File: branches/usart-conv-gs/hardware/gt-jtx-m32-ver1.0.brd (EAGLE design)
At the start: 59.4 x 64.8 mm, 29 parts, among them IC1 MEGA32-P

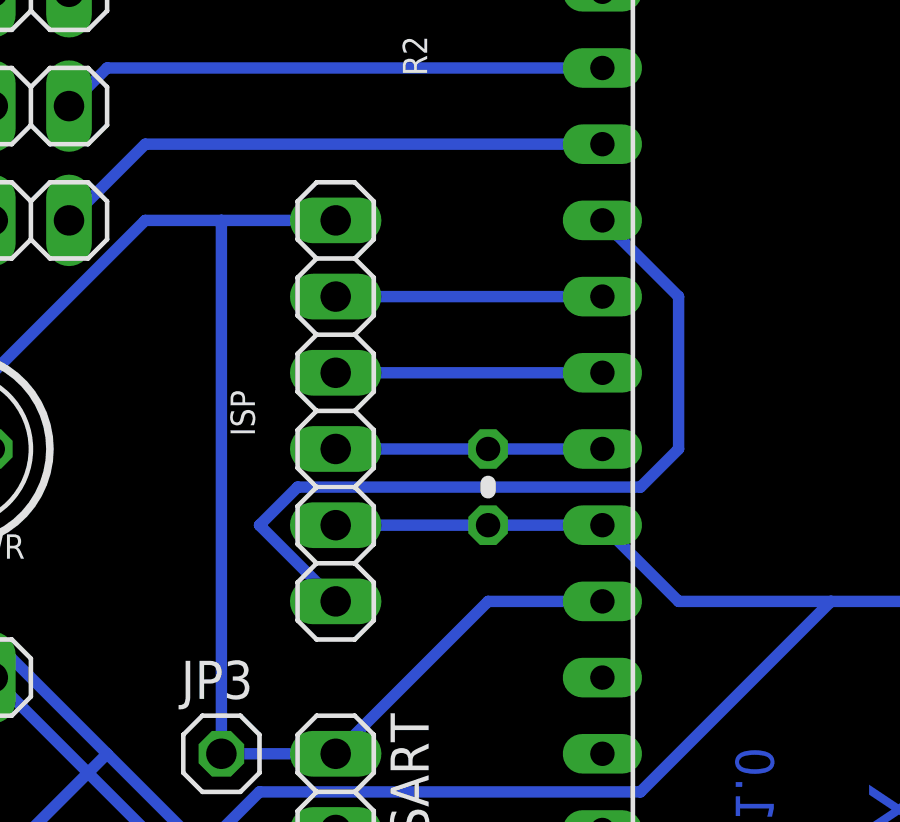
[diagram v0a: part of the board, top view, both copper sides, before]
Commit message: changed pin header to 3x2 instead of 1x6 for accomodating a 6 pin isp. correctec pin configurations
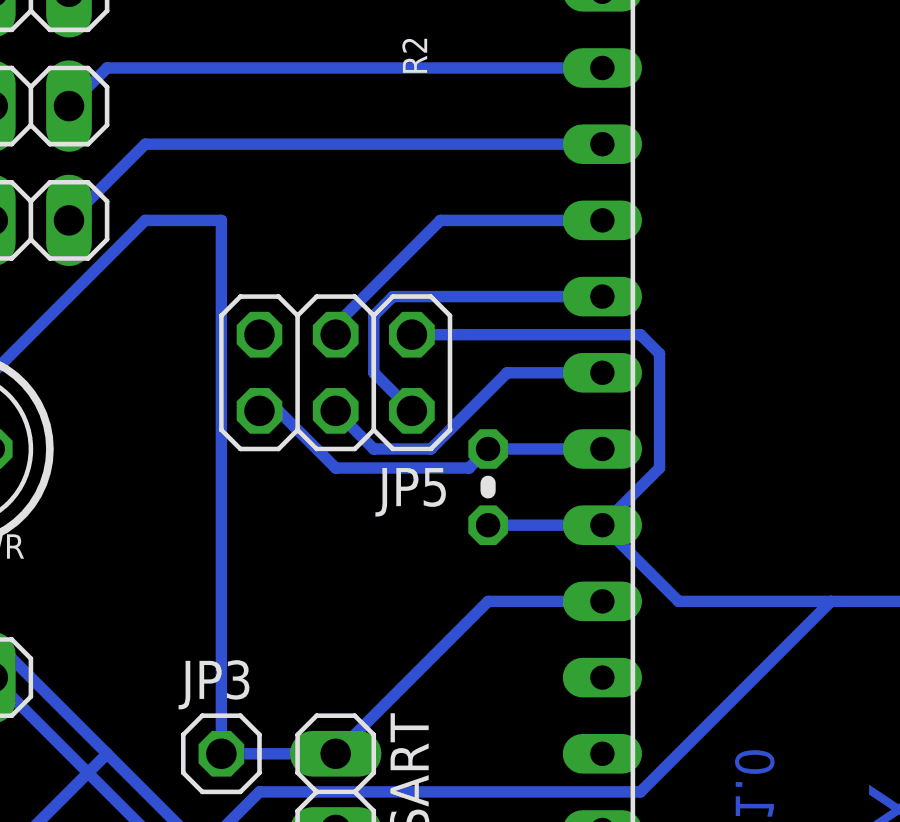
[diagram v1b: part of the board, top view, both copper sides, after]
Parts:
- removed ISP: (no value), pinhead:1X06
- added JP5: (no value), pinhead:2X03
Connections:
- net +5V: now also JP5.1; no longer ISP.2
- net GND: now also JP5.5; no longer ISP.6
- net N$12: now also JP5.3; no longer ISP.1
- net N$13: now also JP5.2; no longer ISP.5
- net N$14: now also JP5.4; no longer ISP.4
- net N$9: now also JP5.6; no longer ISP.3
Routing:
- net N$12: track 27.3 -> 10.7 mm
- net +5V: track 229.5 -> 239.5 mm
- net GND: track 231.3 -> 227.5 mm
- net N$9: track 8.89 -> 12.5 mm
- net N$13: track 8.89 -> 11.6 mm
- net N$14: track 8.89 -> 10.5 mm
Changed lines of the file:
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@@
 <?xml version="1.0" encoding="utf-8"?>
 <!DOCTYPE eagle SYSTEM "eagle.dtd">
-<eagle version="6.3">
+<eagle version="7.5.0">
 <drawing>
 <settings>
@@
 <autorouter>
 <pass name="Default">
-<param name="RoutingGrid" value="50mil"/>
+<param name="RoutingGrid" value="12.5mil"/>
+<param name="AutoGrid" value="1"/>
+<param name="Efforts" value="0"/>
+<param name="TopRouterVariant" value="1"/>
 <param name="tpViaShape" value="round"/>
 <param name="PrefDir.1" value="0"/>
@@
 <attribute name="VALUE" x="3.1496" y="36.0934" size="1.27" layer="27" ratio="10" rot="R180"/>
 </element>
-<element name="ISP" library="pinhead" package="1X06" value="" x="19.05" y="35.56" smashed="yes" rot="R90">
-<attribute name="NAME" x="15.9512" y="35.4838" size="0.8128" layer="25" ratio="10" rot="R90" align="center"/>
-<attribute name="VALUE" x="22.225" y="27.94" size="1.27" layer="27" rot="R90"/>
-</element>
 <element name="IC1" library="atmel" package="DIL40" value="MEGA32-P" x="35.56" y="30.48" rot="R270">
 <attribute name="OC_NEWARK" value="51P1794" x="35.56" y="30.48" size="0.8128" layer="27" rot="R270" display="off"/>
@@
 <element name="JP3" library="pinhead" package="1X01" value="" x="15.24" y="24.13"/>
 <element name="JP4" library="pinhead" package="1X01" value="" x="53.34" y="5.08"/>
+<element name="JP5" library="pinhead" package="2X03" value="" x="19.05" y="36.83" rot="R180"/>
 </elements>
 <signals>
@@
 <contactref element="GNDC" pad="7"/>
 <contactref element="GNDC" pad="8"/>
-<contactref element="ISP" pad="6"/>
 <contactref element="AD0" pad="1"/>
 <contactref element="AD1" pad="1"/>
@@
 <wire x1="5.08" y1="41.91" x2="5.08" y2="34.29" width="0.381" layer="16"/>
 <wire x1="12.7" y1="41.91" x2="15.24" y2="41.91" width="0.381" layer="16"/>
-<wire x1="15.24" y1="41.91" x2="19.05" y2="41.91" width="0.381" layer="16"/>
 <wire x1="5.08" y1="34.29" x2="12.7" y2="41.91" width="0.381" layer="16"/>
 <wire x1="5.08" y1="41.91" x2="5.08" y2="45.72" width="0.381" layer="16"/>
@@
 <vertex x="1.27" y="1.27"/>
 </polygon>
+<contactref element="JP5" pad="5"/>
 </signal>
 <signal name="+5V">
@@
 <contactref element="PPM" pad="2"/>
 <contactref element="USART" pad="4"/>
-<contactref element="ISP" pad="2"/>
 <contactref element="D7" pad="2"/>
 <contactref element="D6" pad="2"/>
@@
 <wire x1="7.62" y1="27.94" x2="7.62" y2="26.67" width="0.381" layer="16"/>
 <wire x1="11.43" y1="24.13" x2="7.62" y2="20.32" width="0.381" layer="16"/>
-<wire x1="27.94" y1="31.75" x2="24.13" y2="31.75" width="0.381" layer="16"/>
 <wire x1="30.48" y1="29.21" x2="35.56" y2="29.21" width="0.381" layer="16"/>
 <wire x1="35.56" y1="29.21" x2="38.1" y2="29.21" width="0.381" layer="16"/>
@@
 <wire x1="27.94" y1="31.75" x2="30.48" y2="29.21" width="0.381" layer="16"/>
 <wire x1="38.1" y1="29.21" x2="43.18" y2="34.29" width="0.381" layer="16"/>
-<wire x1="24.13" y1="31.75" x2="19.05" y2="31.75" width="0.381" layer="16"/>
 <wire x1="7.62" y1="45.72" x2="7.62" y2="41.91" width="0.381" layer="16"/>
 <wire x1="7.62" y1="53.34" x2="7.62" y2="49.53" width="0.381" layer="16"/>
@@
 <wire x1="29.21" y1="22.86" x2="16.51" y2="22.86" width="0.381" layer="16"/>
 <wire x1="35.56" y1="29.21" x2="29.21" y2="22.86" width="0.381" layer="16"/>
+<contactref element="JP5" pad="1"/>
+<wire x1="27.94" y1="31.75" x2="24.13" y2="31.75" width="0.381" layer="16"/>
+<wire x1="29.21" y1="38.1" x2="21.59" y2="38.1" width="0.381" layer="16"/>
+<wire x1="29.845" y1="37.465" x2="29.21" y2="38.1" width="0.381" layer="16"/>
+<wire x1="29.845" y1="33.655" x2="29.845" y2="37.465" width="0.381" layer="16"/>
+<wire x1="27.94" y1="31.75" x2="29.845" y2="33.655" width="0.381" layer="16"/>
 </signal>
 <signal name="N$1">
@@
 <contactref element="R2" pad="2"/>
 <contactref element="IC1" pad="9"/>
-<contactref element="ISP" pad="3"/>
+<contactref element="JP5" pad="6"/>
 <wire x1="27.94" y1="34.29" x2="24.13" y2="34.29" width="0.381" layer="16"/>
-<wire x1="24.13" y1="34.29" x2="19.05" y2="34.29" width="0.381" layer="16"/>
+<wire x1="17.145" y1="35.56" x2="16.51" y2="35.56" width="0.381" layer="16"/>
+<wire x1="19.05" y1="33.655" x2="17.145" y2="35.56" width="0.381" layer="16"/>
+<wire x1="23.495" y1="33.655" x2="19.05" y2="33.655" width="0.381" layer="16"/>
+<wire x1="24.13" y1="34.29" x2="23.495" y2="33.655" width="0.381" layer="16"/>
 </signal>
 <signal name="N$13">
 <contactref element="IC1" pad="7"/>
-<contactref element="ISP" pad="5"/>
-<wire x1="19.05" y1="39.37" x2="27.94" y2="39.37" width="0.381" layer="16"/>
+<contactref element="JP5" pad="2"/>
+<wire x1="20.955" y1="39.37" x2="27.94" y2="39.37" width="0.381" layer="16"/>
+<wire x1="20.32" y1="38.735" x2="20.955" y2="39.37" width="0.381" layer="16"/>
+<wire x1="20.32" y1="36.83" x2="20.32" y2="38.735" width="0.381" layer="16"/>
+<wire x1="21.59" y1="35.56" x2="20.32" y2="36.83" width="0.381" layer="16"/>
 </signal>
 <signal name="N$14">
 <contactref element="IC1" pad="8"/>
-<contactref element="ISP" pad="4"/>
-<wire x1="19.05" y1="36.83" x2="27.94" y2="36.83" width="0.381" layer="16"/>
+<contactref element="JP5" pad="4"/>
+<wire x1="24.765" y1="36.83" x2="27.94" y2="36.83" width="0.381" layer="16"/>
+<wire x1="22.225" y1="34.29" x2="24.765" y2="36.83" width="0.381" layer="16"/>
+<wire x1="20.32" y1="34.29" x2="22.225" y2="34.29" width="0.381" layer="16"/>
+<wire x1="19.05" y1="35.56" x2="20.32" y2="34.29" width="0.381" layer="16"/>
 </signal>
 <signal name="N$5">
@@
 <signal name="N$12">
 <contactref element="IC1" pad="6"/>
-<contactref element="ISP" pad="1"/>
-<wire x1="30.48" y1="39.37" x2="27.94" y2="41.91" width="0.381" layer="16"/>
-<wire x1="30.48" y1="34.29" x2="30.48" y2="39.37" width="0.381" layer="16"/>
-<wire x1="29.21" y1="33.02" x2="30.48" y2="34.29" width="0.381" layer="16"/>
-<wire x1="17.78" y1="33.02" x2="29.21" y2="33.02" width="0.381" layer="16"/>
-<wire x1="16.51" y1="31.75" x2="17.78" y2="33.02" width="0.381" layer="16"/>
-<wire x1="19.05" y1="29.21" x2="16.51" y2="31.75" width="0.381" layer="16"/>
+<contactref element="JP5" pad="3"/>
+<wire x1="22.5425" y1="41.91" x2="27.94" y2="41.91" width="0.381" layer="16"/>
+<wire x1="19.05" y1="38.4175" x2="22.5425" y2="41.91" width="0.381" layer="16"/>
+<wire x1="19.05" y1="38.1" x2="19.05" y2="38.4175" width="0.381" layer="16"/>
 </signal>
 </signals>
